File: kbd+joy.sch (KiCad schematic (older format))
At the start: 50 parts, among them CN2 KEYBOARD_HEADER, CN4 JOY1, CN5 JOY2, U11 74LS125, U13 MOS_6529

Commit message: Map RP3/4 and add (J)D1/2
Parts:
- added JD1, JD2: Jumper_3_Bridged12, LittleSixteen:SolderJumper2x, symbol Jumper:Jumper_3_Bridged12
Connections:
- wire segments 222 -> 234
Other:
- note added: "The JD1 and JD2 jumpers are not present\nin the original schematics, but I have traced\nthem on my board. They are labeled "D1" and\n"D2", I have renamed them to avoid conflicts\nwith the diodes bearing the same labels.\n\nTheir purpose seems to be able to enable the\njoysticks after passing through the keyboard\ndriver. Since the latter was introduced late in\nthe C16 architecture, maybe the des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"
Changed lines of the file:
@@
 Sheet 6 11
 Title "LittleSixteen"
-Date "2020-01-03"
+Date "2020-01-20"
 Rev "1git"
 Comp "SukkoPera"
@@
 	6485 1480 6485 2680
 Wire Wire Line
-	5865 1680 6665 1680
+	5865 1680 5985 1680
 Wire Wire Line
 	6665 1680 6665 1980
@@
 	7030 1580 7130 1680
 Wire Wire Line
-	5865 1580 6860 1580
+	5865 1580 6090 1580
 Wire Wire Line
 	6860 1580 6860 1530
@@
 	4365 1480 3610 1480
 Wire Wire Line
-	4365 1580 3910 1580
+	4365 1580 3905 1580
 Wire Wire Line
 	4365 1680 4025 1680
@@
 Wire Wire Line
 	5295 3255 5295 3170
-Wire Wire Line
-	4025 1680 4025 2920
-Wire Wire Line
-	4025 2920 4995 2920
 Connection ~ 4025 1680
 Wire Wire Line
@@
 $EndComp
 Wire Wire Line
-	3910 1580 3910 2920
-Wire Wire Line
-	3910 2920 3315 2920
-Wire Wire Line
-	3315 2920 3315 4745
-Connection ~ 3910 1580
-Wire Wire Line
-	3910 1580 3610 1580
-Wire Wire Line
-	3315 4745 3555 4745
+	3905 1580 3905 2510
+Connection ~ 3905 1580
+Wire Wire Line
+	3905 1580 3610 1580
 Wire Wire Line
 	7955 5760 7955 2580
@@
 Wire Wire Line
 	6685 6295 8315 6295
+Wire Wire Line
+	4765 2920 4995 2920
+Wire Wire Line
+	3905 2510 2775 2510
+Wire Wire Line
+	4025 3270 4615 3270
+Wire Wire Line
+	4615 3270 4615 3170
+Wire Wire Line
+	4025 1680 4025 3270
+Wire Wire Line
+	5985 1680 5985 2510
+Wire Wire Line
+	5985 2510 4615 2510
+Wire Wire Line
+	4615 2510 4615 2670
+Connection ~ 5985 1680
+Wire Wire Line
+	5985 1680 6665 1680
+Wire Wire Line
+	6090 1580 6090 2410
+Connection ~ 6090 1580
+Wire Wire Line
+	6090 1580 6860 1580
+Wire Wire Line
+	3320 4745 3555 4745
+Wire Wire Line
+	2775 5110 3170 5110
+Wire Wire Line
+	3170 5110 3170 4995
+Wire Wire Line
+	2775 2510 2775 5110
+Wire Wire Line
+	6090 2410 3170 2410
+Wire Wire Line
+	3170 2410 3170 4495
+Text Notes 2700 4005 2    50   ~ 0
+The JD1 and JD2 jumpers are not present\nin the original schematics, but I have traced\nthem on my board. They are labeled "D1" and\n"D2", I have renamed them to avoid conflicts\nwith the diodes bearing the same labels.\n\nTheir purpose seems to be able to enable the\njoysticks after passing through the keyboard\ndriver. Since the latter was introduced late in\nthe C16 architecture, maybe the designers\nweren't sure what was best and they kept \nboth possibilities.
+$Comp
+L Jumper:Jumper_3_Bridged12 JD2
+U 1 1 5E31F2CA
+P 4615 2920
+F 0 "JD2" V 4615 2987 50  0000 L CNN
+F 1 "Jumper_3_Bridged12" V 4660 2987 50  0001 L CNN
+F 2 "LittleSixteen:SolderJumper2x" H 4615 2920 50  0001 C CNN
+F 3 "~" H 4615 2920 50  0001 C CNN
+	1    4615 2920
+	0    -1   -1   0
+$EndComp
+$Comp
+L Jumper:Jumper_3_Bridged12 JD1
+U 1 1 5E450B9C
+P 3170 4745
+F 0 "JD1" V 3170 4812 50  0000 L CNN
+F 1 "Jumper_3_Bridged12" V 3215 4812 50  0001 L CNN
+F 2 "LittleSixteen:SolderJumper2x" H 3170 4745 50  0001 C CNN
+F 3 "~" H 3170 4745 50  0001 C CNN
+	1    3170 4745
+	0    -1   -1   0
+$EndComp
 Wire Bus Line
 	3510 1380 3510 2085

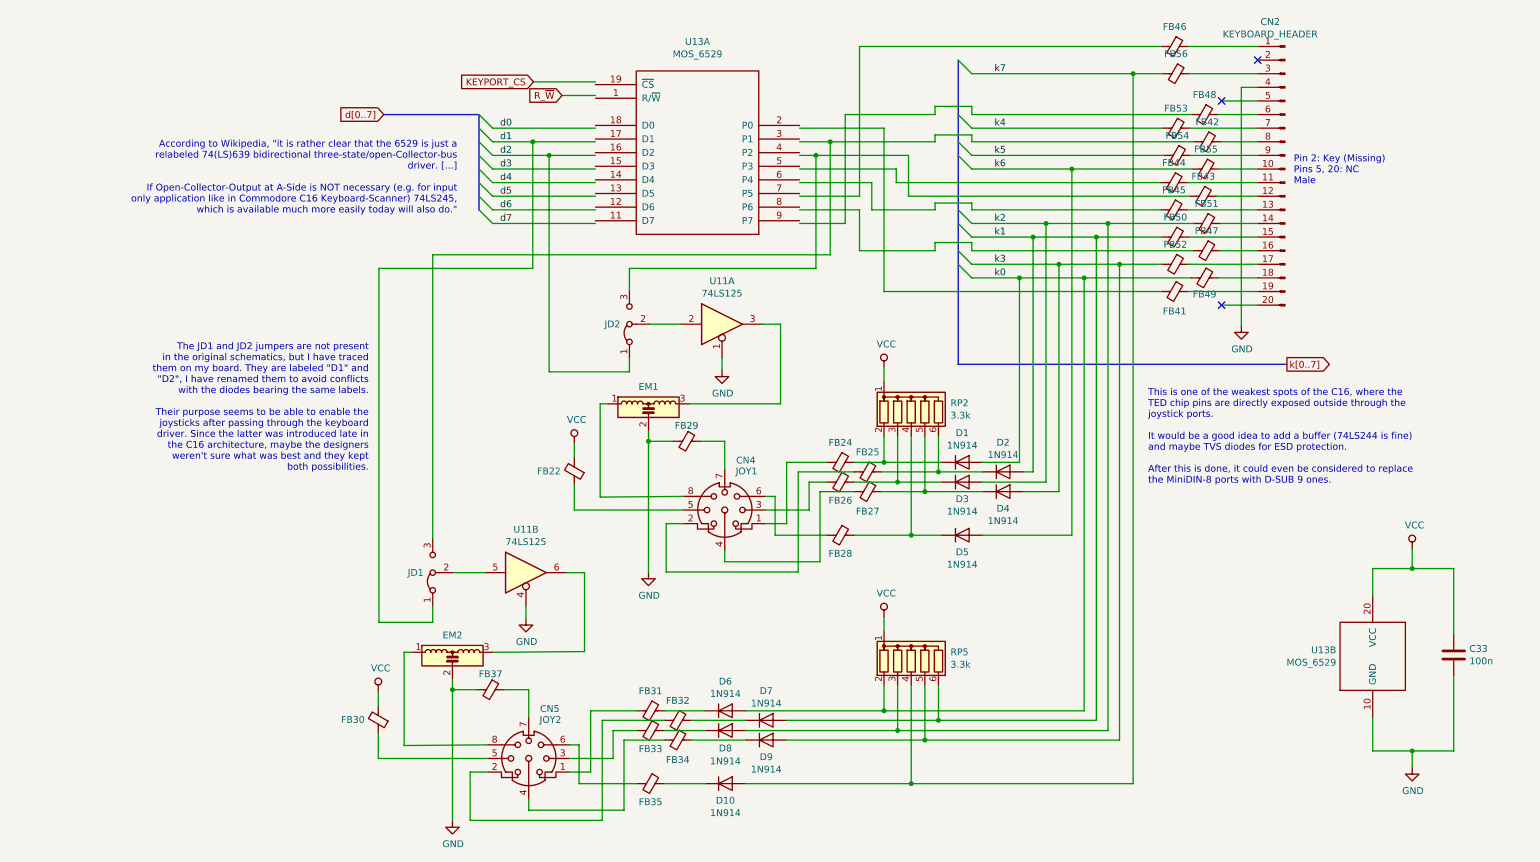
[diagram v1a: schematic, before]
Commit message: cleanup keyboard and joystick schematics
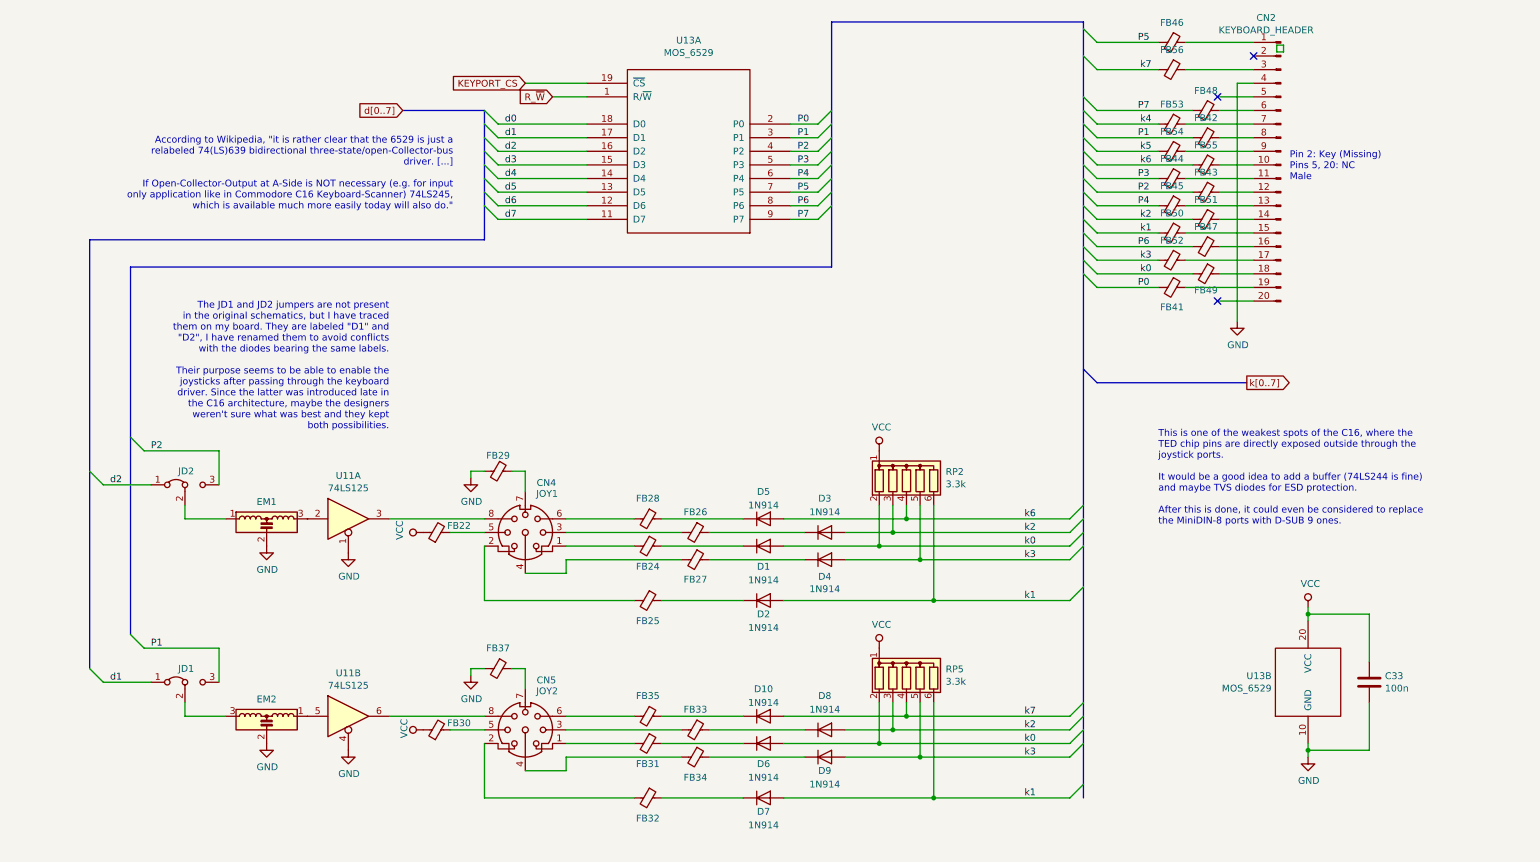
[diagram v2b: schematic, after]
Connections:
- net labels added: P0, P1, P2, P3, P4, P5, P6, P7
- wire segments 234 -> 144
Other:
- moved on the sheet: C33, CN2, CN4, CN5, D1, D10, D2, D3, D4, D5, D6, D7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
